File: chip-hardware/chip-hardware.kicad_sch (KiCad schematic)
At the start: 22 parts, among them J1 Barrel_Jack, J2 Screw_Terminal_01x02, J3 Conn_01x02, U1 TLV70033_SOT23-5, U2 LIS3DH, U3 INA260, U4 MCP9808_MSOP, U5 ESP32-WROOM-32

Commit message: Removed the connection to power for the SDO pin. This means that the LSB will be set to the default address. No errors in the ECE
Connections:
- net +3V3: no longer R3.1, U2.7 (SDO/SA0)
- new net: R3.1, U2.7 (SDO/SA0)
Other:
- note added: "SDO pulled low to set I2C address LSB to 0"
- moved on the sheet: C1, C2, R3, U1

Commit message: Added actual part associations for PCB, started work on PCB
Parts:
- C1, C2: footprint (none) -> Capacitor_SMD:C_0603_1608Metric_Pad1.08x0.95mm_HandSolder
- J1: footprint (none) -> Connector_BarrelJack:BarrelJack_SwitchcraftConxall_RAPC10U_Horizontal
- J2: footprint (none) -> TerminalBlock_RND:TerminalBlock_RND_205-00232_1x02_P5.08mm_Horizontal
- J3: footprint (none) -> Connector_Wire:SolderWire-0.1sqmm_1x02_P3.6mm_D0.4mm_OD1mm
- R1, R10, R11, R12, R2, R3, R4, R5, R6, R7, R8, R9: footprint (none) -> Resistor_SMD:R_0201_0603Metric
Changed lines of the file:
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@@
       (effects (font (size 1.27 1.27)) (justify left))
     )
-    (property "Footprint" "" (id 2) (at 177.292 128.27 90)
+    (property "Footprint" "Resistor_SMD:R_0201_0603Metric" (id 2) (at 177.292 128.27 90)
       (effects (font (size 1.27 1.27)) hide)
     )
@@
       (effects (font (size 1.27 1.27)) (justify left))
     )
-    (property "Footprint" "" (id 2) (at 149.352 172.72 90)
+    (property "Footprint" "Resistor_SMD:R_0201_0603Metric" (id 2) (at 149.352 172.72 90)
       (effects (font (size 1.27 1.27)) hide)
     )
@@
       (effects (font (size 1.27 1.27)) (justify left))
     )
-    (property "Footprint" "" (id 2) (at 41.6052 148.59 0)
+    (property "Footprint" "Capacitor_SMD:C_0603_1608Metric_Pad1.08x0.95mm_HandSolder" (id 2) (at 41.6052 148.59 0)
       (effects (font (size 1.27 1.27)) hide)
     )
@@
       (effects (font (size 1.27 1.27)) (justify left))
     )
-    (property "Footprint" "" (id 2) (at 131.572 46.99 90)
+    (property "Footprint" "Resistor_SMD:R_0201_0603Metric" (id 2) (at 131.572 46.99 90)
       (effects (font (size 1.27 1.27)) hide)
     )
@@
       (effects (font (size 1.27 1.27)) (justify left))
     )
-    (property "Footprint" "" (id 2) (at 56.642 63.5 90)
+    (property "Footprint" "Resistor_SMD:R_0201_0603Metric" (id 2) (at 56.642 63.5 90)
       (effects (font (size 1.27 1.27)) hide)
     )
@@
     (property "Reference" "J2" (id 0) (at 91.44 147.32 0))
     (property "Value" "Screw_Terminal_01x02" (id 1) (at 91.44 149.86 0))
-    (property "Footprint" "" (id 2) (at 91.44 156.21 0)
+    (property "Footprint" "TerminalBlock_RND:TerminalBlock_RND_205-00232_1x02_P5.08mm_Horizontal" (id 2) (at 91.44 156.21 0)
       (effects (font (size 1.27 1.27)) hide)
     )
@@
       (effects (font (size 1.27 1.27)) (justify left))
     )
-    (property "Footprint" "" (id 2) (at 121.412 82.55 90)
+    (property "Footprint" "Resistor_SMD:R_0201_0603Metric" (id 2) (at 121.412 82.55 90)
       (effects (font (size 1.27 1.27)) hide)
     )
@@
     (property "Reference" "J1" (id 0) (at 22.86 154.94 0))
     (property "Value" "Barrel_Jack" (id 1) (at 22.86 157.48 0))
-    (property "Footprint" "" (id 2) (at 24.13 164.846 0)
+    (property "Footprint" "Connector_BarrelJack:BarrelJack_SwitchcraftConxall_RAPC10U_Horizontal" (id 2) (at 24.13 164.846 0)
       (effects (font (size 1.27 1.27)) hide)
     )
@@
       (effects (font (size 1.27 1.27)) (justify left))
     )
-    (property "Footprint" "" (id 2) (at 27.432 38.1 90)
+    (property "Footprint" "Resistor_SMD:R_0201_0603Metric" (id 2) (at 27.432 38.1 90)
       (effects (font (size 1.27 1.27)) hide)
     )
@@
       (effects (font (size 1.27 1.27)) (justify left))
     )
-    (property "Footprint" "" (id 2) (at 269.24 69.85 0)
+    (property "Footprint" "Connector_Wire:SolderWire-0.1sqmm_1x02_P3.6mm_D0.4mm_OD1mm" (id 2) (at 269.24 69.85 0)
       (effects (font (size 1.27 1.27)) hide)
     )
@@
       (effects (font (size 1.27 1.27)) (justify left))
     )
-    (property "Footprint" "" (id 2) (at 120.142 46.99 90)
+    (property "Footprint" "Resistor_SMD:R_0201_0603Metric" (id 2) (at 120.142 46.99 90)
       (effects (font (size 1.27 1.27)) hide)
     )
@@
       (effects (font (size 1.27 1.27)) (justify left))
     )
-    (property "Footprint" "" (id 2) (at 38.862 38.1 90)
+    (property "Footprint" "Resistor_SMD:R_0201_0603Metric" (id 2) (at 38.862 38.1 90)
       (effects (font (size 1.27 1.27)) hide)
     )
@@
       (effects (font (size 1.27 1.27)) (justify left))
     )
-    (property "Footprint" "" (id 2) (at 130.302 82.55 90)
+    (property "Footprint" "Resistor_SMD:R_0201_0603Metric" (id 2) (at 130.302 82.55 90)
       (effects (font (size 1.27 1.27)) hide)
     )
@@
       (effects (font (size 1.27 1.27)) (justify left))
     )
-    (property "Footprint" "" (id 2) (at 160.782 172.72 90)
+    (property "Footprint" "Resistor_SMD:R_0201_0603Metric" (id 2) (at 160.782 172.72 90)
       (effects (font (size 1.27 1.27)) hide)
     )
@@
       (effects (font (size 1.27 1.27)) (justify left))
     )
-    (property "Footprint" "" (id 2) (at 69.5452 148.59 0)
+    (property "Footprint" "Capacitor_SMD:C_0603_1608Metric_Pad1.08x0.95mm_HandSolder" (id 2) (at 69.5452 148.59 0)
       (effects (font (size 1.27 1.27)) hide)
     )
@@
       (effects (font (size 1.27 1.27)) (justify left))
     )
-    (property "Footprint" "" (id 2) (at 139.192 82.55 90)
+    (property "Footprint" "Resistor_SMD:R_0201_0603Metric" (id 2) (at 139.192 82.55 90)
       (effects (font (size 1.27 1.27)) hide)
     )
@@
       (effects (font (size 1.27 1.27)) (justify left))
     )
-    (property "Footprint" "" (id 2) (at 165.862 128.27 90)
+    (property "Footprint" "Resistor_SMD:R_0201_0603Metric" (id 2) (at 165.862 128.27 90)
       (effects (font (size 1.27 1.27)) hide)
     )
@@
     )
     (path "/2aabdce3-989b-4fb0-b6be-0f4503b5a90f"
-      (reference "C1") (unit 1) (value "10uF") (footprint "")
+      (reference "C1") (unit 1) (value "10uF") (footprint "Capacitor_SMD:C_0603_1608Metric_Pad1.08x0.95mm_HandSolder")
     )
     (path "/e77b9723-376d-4560-be0d-26563be50d83"
-      (reference "C2") (unit 1) (value "1uF") (footprint "")
+      (reference "C2") (unit 1) (value "1uF") (footprint "Capacitor_SMD:C_0603_1608Metric_Pad1.08x0.95mm_HandSolder")
     )
     (path "/93f9a4ec-6178-4177-96ea-b1e29968ed97"
-      (reference "J1") (unit 1) (value "Barrel_Jack") (footprint "")
+      (reference "J1") (unit 1) (value "Barrel_Jack") (footprint "Connector_BarrelJack:BarrelJack_SwitchcraftConxall_RAPC10U_Horizontal")
     )
     (path "/8e18a617-8fde-484c-8e84-b1cb60f91fba"
-      (reference "J2") (unit 1) (value "Screw_Terminal_01x02") (footprint "")
+      (reference "J2") (unit 1) (value "Screw_Terminal_01x02") (footprint "TerminalBlock_RND:TerminalBlock_RND_205-00232_1x02_P5.08mm_Horizontal")
     )
     (path "/b85702f6-44e3-4138-82c9-c5f12635d1fd"
-      (reference "J3") (unit 1) (value "Conn_01x02") (footprint "")
+      (reference "J3") (unit 1) (value "Conn_01x02") (footprint "Connector_Wire:SolderWire-0.1sqmm_1x02_P3.6mm_D0.4mm_OD1mm")
     )
     (path "/b1cd3c0d-213f-4dc1-be26-766713e727fa"
-      (reference "R1") (unit 1) (value "10k") (footprint "")
+      (reference "R1") (unit 1) (value "10k") (footprint "Resistor_SMD:R_0201_0603Metric")
     )
     (path "/cef56e10-d1da-4750-bce4-cd8b2ed6e102"
-      (reference "R2") (unit 1) (value "10k") (footprint "")
+      (reference "R2") (unit 1) (value "10k") (footprint "Resistor_SMD:R_0201_0603Metric")
     )
     (path "/69ba1daf-84c8-4818-9442-655ca06f4d26"
-      (reference "R3") (unit 1) (value "10k") (footprint "")
+      (reference "R3") (unit 1) (value "10k") (footprint "Resistor_SMD:R_0201_0603Metric")
     )
     (path "/c05d7c3e-8ddd-4b2a-ba0e-5008024d10ed"
-      (reference "R4") (unit 1) (value "10k") (footprint "")
+      (reference "R4") (unit 1) (value "10k") (footprint "Resistor_SMD:R_0201_0603Metric")
     )
     (path "/8e462e04-f332-48bc-8ddd-b513e4188cfd"
-      (reference "R5") (unit 1) (value "10k") (footprint "")
+      (reference "R5") (unit 1) (value "10k") (footprint "Resistor_SMD:R_0201_0603Metric")
     )
     (path "/d7f04a8b-1fee-4e24-8865-e6f87ee89761"
-      (reference "R6") (unit 1) (value "10k") (footprint "")
+      (reference "R6") (unit 1) (value "10k") (footprint "Resistor_SMD:R_0201_0603Metric")
     )
     (path "/5c492b92-1286-4e16-bec8-02de645ee094"
-      (reference "R7") (unit 1) (value "10k") (footprint "")
+      (reference "R7") (unit 1) (value "10k") (footprint "Resistor_SMD:R_0201_0603Metric")
     )
     (path "/ed884843-773f-49ac-8eb1-1345196a97f3"
-      (reference "R8") (unit 1) (value "10k") (footprint "")
+      (reference "R8") (unit 1) (value "10k") (footprint "Resistor_SMD:R_0201_0603Metric")
     )
     (path "/27846c45-c90b-4d61-b729-38ad6cd0463a"
-      (reference "R9") (unit 1) (value "10k") (footprint "")
+      (reference "R9") (unit 1) (value "10k") (footprint "Resistor_SMD:R_0201_0603Metric")
     )
     (path "/d8e2c9af-f9ce-4503-a304-fb81566d1947"
-      (reference "R10") (unit 1) (value "10k") (footprint "")
+      (reference "R10") (unit 1) (value "10k") (footprint "Resistor_SMD:R_0201_0603Metric")
     )
     (path "/f77af766-7e7f-4553-a69e-2664c11e3bea"
-      (reference "R11") (unit 1) (value "10k") (footprint "")
+      (reference "R11") (unit 1) (value "10k") (footprint "Resistor_SMD:R_0201_0603Metric")
     )
     (path "/2427fd03-1446-4bc2-9334-9ca91f0de036"
-      (reference "R12") (unit 1) (value "10k") (footprint "")
+      (reference "R12") (unit 1) (value "10k") (footprint "Resistor_SMD:R_0201_0603Metric")
     )
     (path "/96d16543-2140-444f-8d7a-380470ae31ed"

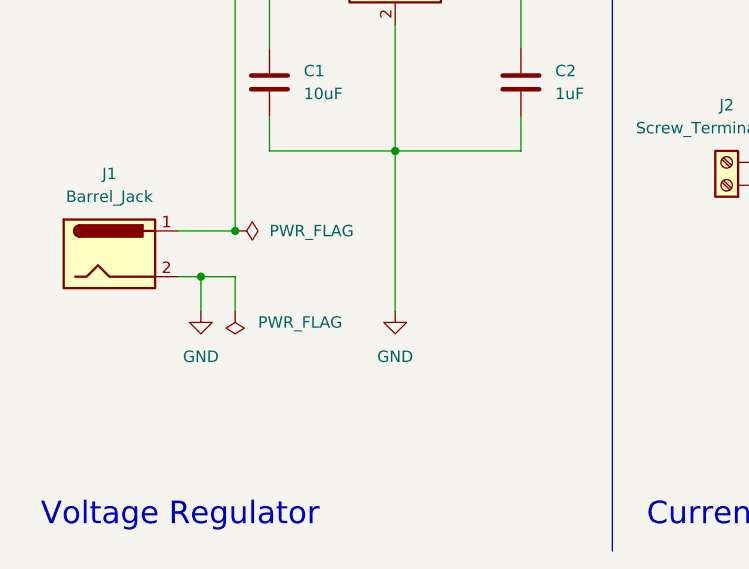
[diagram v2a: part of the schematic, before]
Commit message: pulled in pretty format for new barrel jack connector
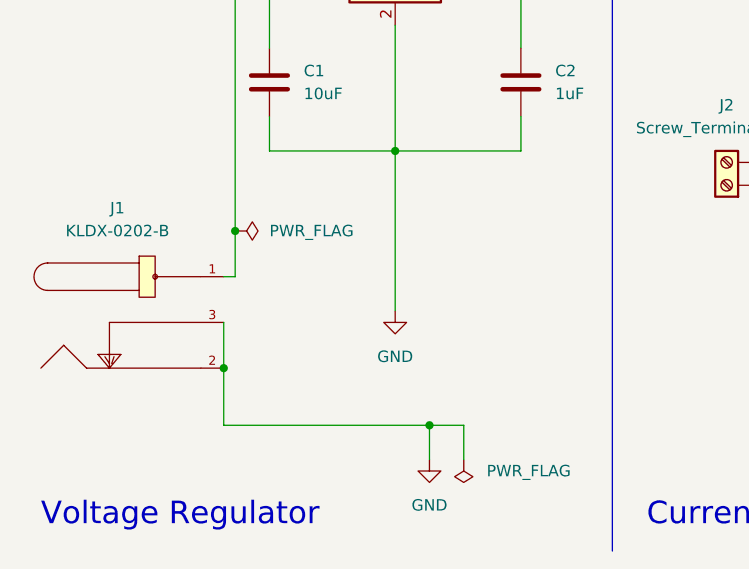
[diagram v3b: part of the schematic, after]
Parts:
- removed J1: Barrel_Jack, Connector_BarrelJack:BarrelJack_SwitchcraftConxall_RAPC10U_Horizontal, symbol Connector:Barrel_Jack
- added J1: KLDX-0202-B, eec:Kycon-KLDX-0202-B-MFG, symbol eec:KLDX-0202-B
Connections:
- net GND: now also J1.2, J1.3
- net at C1.1, U1.1 (IN), U1.3 (EN): now also J1.1
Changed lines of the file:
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@@
   (junction (at 152.4 58.42) (diameter 0) (color 0 0 0 0)
   )
+  (junction (at 35.56 176.53) (diameter 0) (color 0 0 0 0)
+  )
   (junction (at 34.29 53.34) (diameter 0) (color 0 0 0 0)
   )
@@
   (junction (at 80.01 33.02) (diameter 0) (color 0 0 0 0)
   )
+  (junction (at 36.83 161.29) (diameter 0) (color 0 0 0 0)
+  )
   (junction (at 54.61 152.4) (diameter 0) (color 0 0 0 0)
   )
-  (junction (at 36.83 161.29) (diameter 0) (color 0 0 0 0)
-  )
-  (junction (at 33.02 166.37) (diameter 0) (color 0 0 0 0)
+  (junction (at 58.42 182.88) (diameter 0) (color 0 0 0 0)
   )
   (junction (at 40.64 33.02) (diameter 0) (color 0 0 0 0)
@@
     (stroke (width 0) (type default) (color 0 0 0 0))
   )
-  (wire (pts (xy 36.83 166.37) (xy 33.02 166.37))
+  (wire (pts (xy 62.23 182.88) (xy 58.42 182.88))
     (stroke (width 0) (type default) (color 0 0 0 0))
   )
@@
     (stroke (width 0) (type default) (color 0 0 0 0))
   )
-  (wire (pts (xy 30.48 166.37) (xy 33.02 166.37))
+  (wire (pts (xy 35.56 182.88) (xy 58.42 182.88))
     (stroke (width 0) (type default) (color 0 0 0 0))
   )
@@
     (stroke (width 0) (type default) (color 0 0 0 0))
   )
+  (wire (pts (xy 35.56 171.45) (xy 35.56 176.53))
+    (stroke (width 0) (type default) (color 0 0 0 0))
+  )
   (wire (pts (xy 140.97 86.36) (xy 140.97 91.44))
     (stroke (width 0) (type default) (color 0 0 0 0))
@@
     (stroke (width 0) (type default) (color 0 0 0 0))
   )
+  (wire (pts (xy 35.56 176.53) (xy 35.56 182.88))
+    (stroke (width 0) (type default) (color 0 0 0 0))
+  )
   (wire (pts (xy 172.72 34.29) (xy 172.72 50.8))
     (stroke (width 0) (type default) (color 0 0 0 0))
@@
     (stroke (width 0) (type default) (color 0 0 0 0))
   )
-  (wire (pts (xy 33.02 166.37) (xy 33.02 170.18))
+  (wire (pts (xy 58.42 182.88) (xy 58.42 186.69))
     (stroke (width 0) (type default) (color 0 0 0 0))
   )
@@
     (stroke (width 0) (type default) (color 0 0 0 0))
   )
+  (wire (pts (xy 36.83 166.37) (xy 35.56 166.37))
+    (stroke (width 0) (type default) (color 0 0 0 0))
+  )
+  (wire (pts (xy 36.83 161.29) (xy 36.83 166.37))
+    (stroke (width 0) (type default) (color 0 0 0 0))
+  )
   (wire (pts (xy 151.13 176.53) (xy 151.13 182.88))
     (stroke (width 0) (type default) (color 0 0 0 0))
@@
     (stroke (width 0) (type default) (color 0 0 0 0))
   )
-  (wire (pts (xy 36.83 161.29) (xy 30.48 161.29))
-    (stroke (width 0) (type default) (color 0 0 0 0))
-  )
   (wire (pts (xy 123.19 66.04) (xy 123.19 78.74))
     (stroke (width 0) (type default) (color 0 0 0 0))
@@
     (stroke (width 0) (type default) (color 0 0 0 0))
   )
-  (wire (pts (xy 36.83 170.18) (xy 36.83 166.37))
+  (wire (pts (xy 62.23 186.69) (xy 62.23 182.88))
     (stroke (width 0) (type default) (color 0 0 0 0))
   )
@@
   (label "SCL" (at 264.16 104.14 0)
     (effects (font (size 1.27 1.27)) (justify left bottom))
+  )
+  (symbol (lib_id "eec:KLDX-0202-B") (at 38.1 166.37 0) (unit 1)
+    (in_bom yes) (on_board yes) (fields_autoplaced)
+    (property "Reference" "J1" (id 0) (at 23.749 158.75 0))
+    (property "Value" "KLDX-0202-B" (id 1) (at 23.749 161.29 0))
+    (property "Footprint" "eec:Kycon-KLDX-0202-B-MFG" (id 2) (at 38.1 156.21 0)
+      (effects (font (size 1.27 1.27)) (justify left) hide)
+    )
+    (property "Datasheet" "http://www.kycon.com/2013Catalogpage/DC%20Power/KLDX_0202_LT.pdf" (id 3) (at 38.1 153.67 0)
+      (effects (font (size 1.27 1.27)) (justify left) hide)
+    )
+    (property "automotive" "No" (id 4) (at 38.1 151.13 0)
+      (effects (font (size 1.27 1.27)) (justify left) hide)
+    )
+    (property "category" "Conn" (id 5) (at 38.1 148.59 0)
+      (effects (font (size 1.27 1.27)) (justify left) hide)
+    )
+    (property "contact material" "Nickel" (id 6) (at 38.1 146.05 0)
+      (effects (font (size 1.27 1.27)) (justify left) hide)
+    )
+    (property "current rating" "3.5A" (id 7) (at 38.1 143.51 0)
+      (effects (font (size 1.27 1.27)) (justify left) hide)
+    )
+    (property "device class L1" "Connectors" (id 8) (at 38.1 140.97 0)
+      (effects (font (size 1.27 1.27)) (justify left) hide)
+    )
+    (property "device class L2" "Power Connectors" (id 9) (at 38.1 138.43 0)
+      (effects (font (size 1.27 1.27)) (justify left) hide)
+    )
+    (property "device class L3" "unset" (id 10) (at 38.1 135.89 0)
+      (effects (font (size 1.27 1.27)) (justify left) hide)
+    )
+    (property "digikey description" "CONN PWR JACK 2.5X5.5MM SOLDER" (id 11) (at 38.1 133.35 0)
+      (effects (font (size 1.27 1.27)) (justify left) hide)
+    )
+    (property "digikey part number" "2092-KLDX-0202-B-ND" (id 12) (at 38.1 130.81 0)
+      (effects (font (size 1.27 1.27)) (justify left) hide)
+    )
+    (property "footprint url" "https://www.kycon.com/Pub_Eng_Draw/KLDX-0202-x.pdf" (id 13) (at 38.1 128.27 0)
+      (effects (font (size 1.27 1.27)) (justify left) hide)
+    )
+    (property "height" "11.1mm" (id 14) (at 38.1 125.73 0)
+      (effects (font (size 1.27 1.27)) (justify left) hide)
+    )
+    (property "lead free" "Yes" (id 15) (at 38.1 123.19 0)
+      (effects (font (size 1.27 1.27)) (justify left) hide)
+    )
+    (property "library id" "4c2acf28b9a06429" (id 16) (at 38.1 120.65 0)
+      (effects (font (size 1.27 1.27)) (justify left) hide)
+    )
+    (property "manufacturer" "Kycon" (id 17) (at 38.1 118.11 0)
+      (effects (font (size 1.27 1.27)) (justify left) hide)
+    )
+    (property "mouser description" "Conn Power PIN 2 POS Solder RA Thru-Hole 3 Terminal 1 Port" (id 18) (at 38.1 115.57 0)
+      (effects (font (size 1.27 1.27)) (justify left) hide)
+    )
+    (property "mouser part number" "806-KLDX-0202-B" (id 19) (at 38.1 113.03 0)
+      (effects (font (size 1.27 1.27)) (justify left) hide)
+    )
+    (property "number of contacts" "1" (id 20) (at 38.1 110.49 0)
+      (effects (font (size 1.27 1.27)) (justify left) hide)
+    )
+    (property "package" "CONN_POWER_9MM0_14MM5" (id 21) (at 38.1 107.95 0)
+      (effects (font (size 1.27 1.27)) (justify left) hide)
+    )
+    (property "rohs" "Yes" (id 22) (at 38.1 105.41 0)
+      (effects (font (size 1.27 1.27)) (justify left) hide)
+    )
+    (property "temperature range high" "+85°C" (id 23) (at 38.1 102.87 0)
+      (effects (font (size 1.27 1.27)) (justify left) hide)
+    )
+    (property "temperature range low" "-25°C" (id 24) (at 38.1 100.33 0)
+      (effects (font (size 1.27 1.27)) (justify left) hide)
+    )
+    (property "voltage rating" "24V" (id 25) (at 38.1 97.79 0)
+      (effects (font (size 1.27 1.27)) (justify left) hide)
+    )
+    (pin "1")
+    (pin "2")
+    (pin "3")
   )
   (symbol (lib_id "power:GND") (at 238.76 149.86 0) (unit 1)
@@
     )
     (property "Datasheet" "~" (id 3) (at 123.19 82.55 0)
-      (effects (font (size 1.27 1.27)) hide)
-    )
-    (pin "1")
-    (pin "2")
-  )
-  (symbol (lib_id "Connector:Barrel_Jack") (at 22.86 163.83 0) (unit 1)
-    (in_bom yes) (on_board yes) (fields_autoplaced)
-    (property "Reference" "J1" (id 0) (at 22.86 154.94 0))
-    (property "Value" "Barrel_Jack" (id 1) (at 22.86 157.48 0))
-    (property "Footprint" "Connector_BarrelJack:BarrelJack_SwitchcraftConxall_RAPC10U_Horizontal" (id 2) (at 24.13 164.846 0)
-      (effects (font (size 1.27 1.27)) hide)
-    )
-    (property "Datasheet" "~" (id 3) (at 24.13 164.846 0)
       (effects (font (size 1.27 1.27)) hide)
     )
@@
     (pin "9")
   )
-  (symbol (lib_id "power:GND") (at 33.02 170.18 0) (unit 1)
-    (in_bom yes) (on_board yes) (fields_autoplaced)
-    (property "Reference" "#PWR016" (id 0) (at 33.02 176.53 0)
-      (effects (font (size 1.27 1.27)) hide)
-    )
-    (property "Value" "GND" (id 1) (at 33.02 175.26 0))
-    (property "Footprint" "" (id 2) (at 33.02 170.18 0)
-      (effects (font (size 1.27 1.27)) hide)
-    )
-    (property "Datasheet" "" (id 3) (at 33.02 170.18 0)
+  (symbol (lib_id "power:GND") (at 58.42 186.69 0) (unit 1)
+    (in_bom yes) (on_board yes) (fields_autoplaced)
+    (property "Reference" "#PWR016" (id 0) (at 58.42 193.04 0)
+      (effects (font (size 1.27 1.27)) hide)
+    )
+    (property "Value" "GND" (id 1) (at 58.42 191.77 0))
+    (property "Footprint" "" (id 2) (at 58.42 186.69 0)
+      (effects (font (size 1.27 1.27)) hide)
+    )
+    (property "Datasheet" "" (id 3) (at 58.42 186.69 0)
       (effects (font (size 1.27 1.27)) hide)
     )
@@
     (pin "2")
   )
-  (symbol (lib_id "power:PWR_FLAG") (at 36.83 170.18 180) (unit 1)
-    (in_bom yes) (on_board yes) (fields_autoplaced)
-    (property "Reference" "#FLG0102" (id 0) (at 36.83 172.085 0)
-      (effects (font (size 1.27 1.27)) hide)
-    )
-    (property "Value" "PWR_FLAG" (id 1) (at 39.37 171.4499 0)
+  (symbol (lib_id "power:PWR_FLAG") (at 62.23 186.69 180) (unit 1)
+    (in_bom yes) (on_board yes) (fields_autoplaced)
+    (property "Reference" "#FLG0102" (id 0) (at 62.23 188.595 0)
+      (effects (font (size 1.27 1.27)) hide)
+    )
+    (property "Value" "PWR_FLAG" (id 1) (at 64.77 187.9599 0)
       (effects (font (size 1.27 1.27)) (justify right))
     )
-    (property "Footprint" "" (id 2) (at 36.83 170.18 0)
-      (effects (font (size 1.27 1.27)) hide)
-    )
-    (property "Datasheet" "~" (id 3) (at 36.83 170.18 0)
+    (property "Footprint" "" (id 2) (at 62.23 186.69 0)
+      (effects (font (size 1.27 1.27)) hide)
+    )
+    (property "Datasheet" "~" (id 3) (at 62.23 186.69 0)
       (effects (font (size 1.27 1.27)) hide)
     )
@@
       (reference "C2") (unit 1) (value "1uF") (footprint "Capacitor_SMD:C_0603_1608Metric_Pad1.08x0.95mm_HandSolder")
     )
-    (path "/93f9a4ec-6178-4177-96ea-b1e29968ed97"
-      (reference "J1") (unit 1) (value "Barrel_Jack") (footprint "Connector_BarrelJack:BarrelJack_SwitchcraftConxall_RAPC10U_Horizontal")
+    (path "/162c5980-20d0-4d03-a440-e851a1cc6acb"
+      (reference "J1") (unit 1) (value "KLDX-0202-B") (footprint "eec:Kycon-KLDX-0202-B-MFG")
     )
     (path "/8e18a617-8fde-484c-8e84-b1cb60f91fba"
